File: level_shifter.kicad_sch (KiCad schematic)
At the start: 4 parts, among them U1 TXS0102QDCURQ1

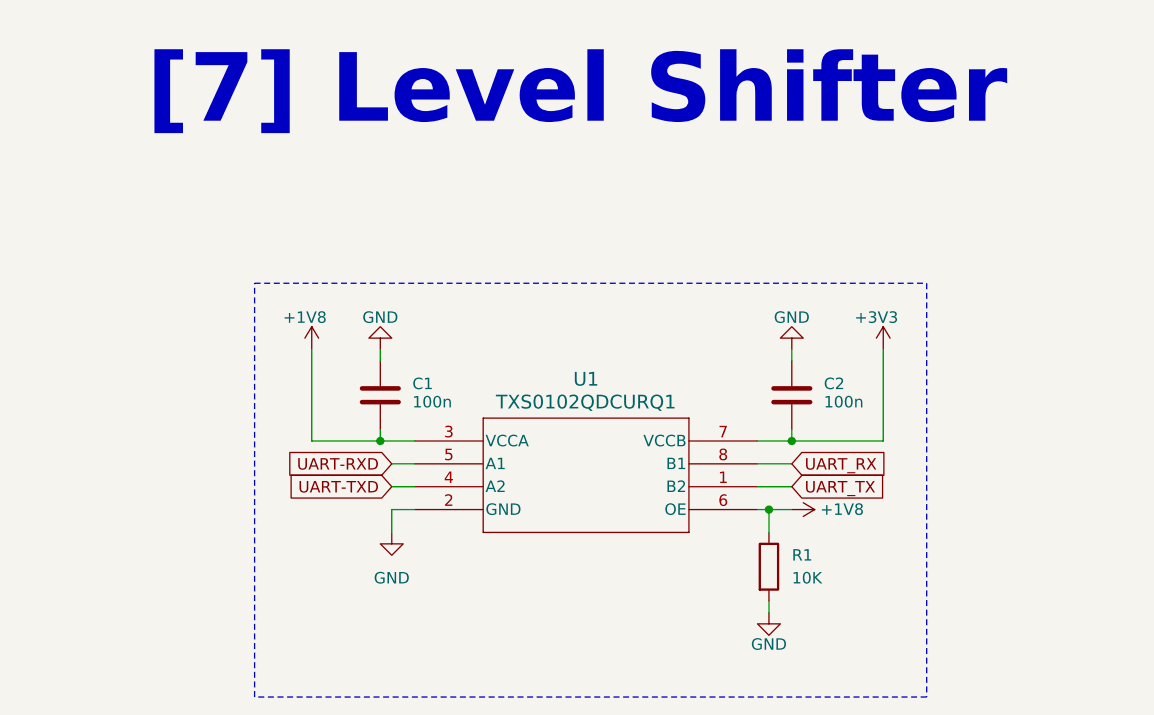
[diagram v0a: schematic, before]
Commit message: Added some decoup caps and reviewed PCB layout
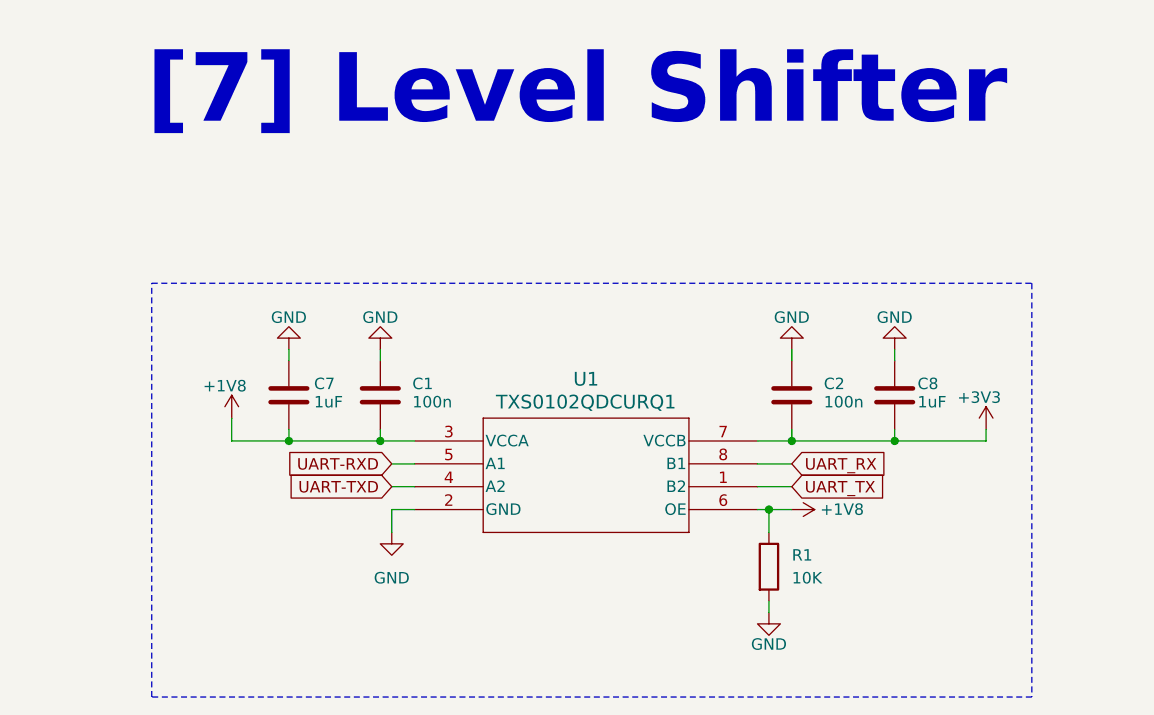
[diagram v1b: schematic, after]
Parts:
- added C7, C8: 1uF, Capacitor_SMD:C_0603_1608Metric, symbol Device:C
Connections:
- net +1V8: now also C7.2
- net +3V3: now also C8.2
- net GND: now also C7.1, C8.1

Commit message: removed some decoup caps because I added to many haha
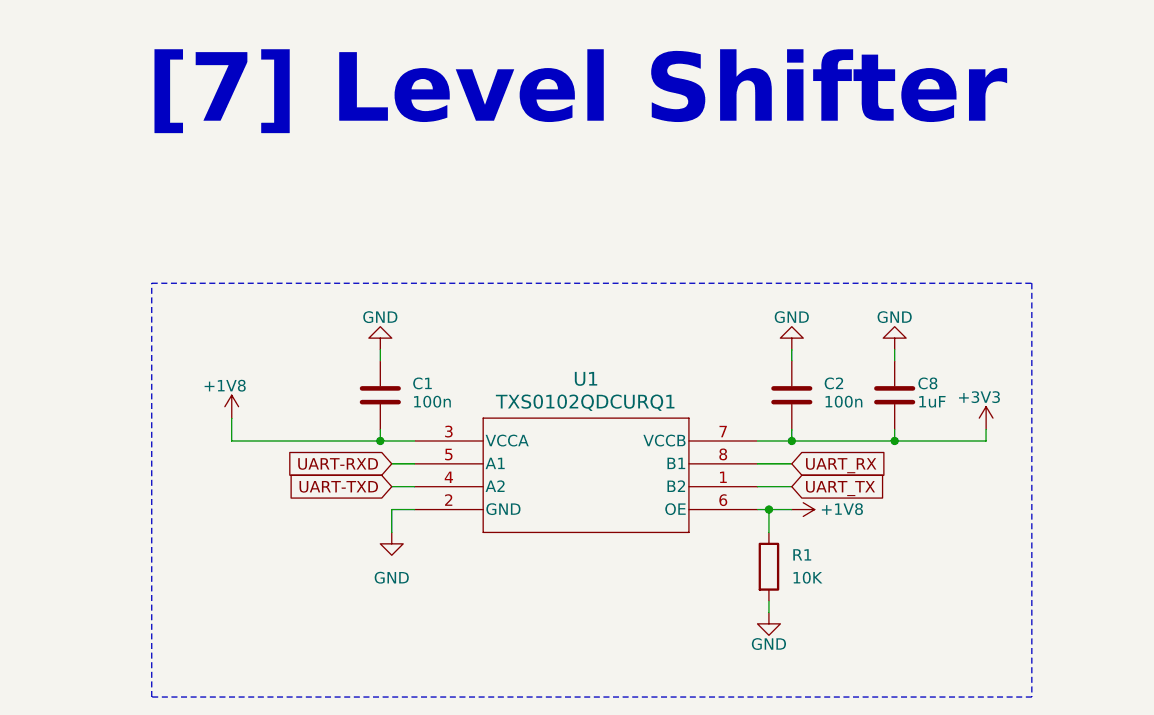
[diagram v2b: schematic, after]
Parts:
- removed C7: 1uF, Capacitor_SMD:C_0603_1608Metric, symbol Device:C
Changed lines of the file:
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@@
 		(color 0 0 0 0)
 	)
-	(junction
-		(at 114.3 69.85)
-		(diameter 0)
-		(color 0 0 0 0)
-	)
 	(wire
 		(pts
@@
 	(wire
 		(pts
-			(xy 114.3 69.85) (xy 124.46 69.85)
+			(xy 107.95 69.85) (xy 124.46 69.85)
 		)
 		(stroke
@@
 	(wire
 		(pts
-			(xy 107.95 69.85) (xy 114.3 69.85)
-		)
-		(stroke
-			(width 0)
-			(type default)
-		)
-	)
-	(wire
-		(pts
 			(xy 166.37 72.39) (xy 170.18 72.39)
 		)
@@
 		(pts
 			(xy 181.61 68.58) (xy 181.61 69.85)
-		)
-		(stroke
-			(width 0)
-			(type default)
-		)
-	)
-	(wire
-		(pts
-			(xy 114.3 59.69) (xy 114.3 60.96)
-		)
-		(stroke
-			(width 0)
-			(type default)
-		)
-	)
-	(wire
-		(pts
-			(xy 114.3 68.58) (xy 114.3 69.85)
 		)
 		(stroke
@@
 	(symbol
 		(lib_id "power:GND")
-		(at 114.3 59.69 180)
-		(unit 1)
-		(body_style 1)
-		(exclude_from_sim no)
-		(in_bom yes)
-		(on_board yes)
-		(in_pos_files yes)
-		(dnp no)
-		(property "Reference" "#PWR046"
-			(at 114.3 53.34 0)
-			(hide yes)
-			(show_name no)
-			(do_not_autoplace no)
-			(effects
-				(font
-					(size 1.27 1.27)
-				)
-			)
-		)
-		(property "Value" "GND"
-			(at 114.3 56.134 0)
-			(show_name no)
-			(do_not_autoplace no)
-			(effects
-				(font
-					(size 1.27 1.27)
-				)
-			)
-		)
-		(property "Footprint" ""
-			(at 114.3 59.69 0)
-			(hide yes)
-			(show_name no)
-			(do_not_autoplace no)
-			(effects
-				(font
-					(size 1.27 1.27)
-				)
-			)
-		)
-		(property "Datasheet" ""
-			(at 114.3 59.69 0)
-			(hide yes)
-			(show_name no)
-			(do_not_autoplace no)
-			(effects
-				(font
-					(size 1.27 1.27)
-				)
-			)
-		)
-		(property "Description" "Power symbol creates a global label with name \"GND\" , ground"
-			(at 114.3 59.69 0)
-			(hide yes)
-			(show_name no)
-			(do_not_autoplace no)
-			(effects
-				(font
-					(size 1.27 1.27)
-				)
-			)
-		)
-		(pin "1"
-		)
-		(instances
-			(project "adapter-pcb"
-				(path "/94da9b83-1146-4f01-8e34-8153765b0257/cf109836-ab8e-48e3-a0ed-36c6666f071e"
-					(reference "#PWR046")
-					(unit 1)
-				)
-			)
-		)
-	)
-	(symbol
-		(lib_id "power:GND")
 		(at 124.46 59.69 180)
 		(unit 1)
@@
 					(unit 1)
 				)
-			)
-		)
-	)
-	(symbol
-		(lib_id "Device:C")
-		(at 114.3 64.77 0)
-		(unit 1)
-		(body_style 1)
-		(exclude_from_sim no)
-		(in_bom yes)
-		(on_board yes)
-		(in_pos_files yes)
-		(dnp no)
-		(property "Reference" "C7"
-			(at 117.094 63.5 0)
-			(show_name no)
-			(do_not_autoplace no)
-			(effects
-				(font
-					(size 1.27 1.27)
-				)
-				(justify left)
-			)
-		)
-		(property "Value" "1uF"
-			(at 117.094 65.532 0)
-			(show_name no)
-			(do_not_autoplace no)
-			(effects
-				(font
-					(size 1.27 1.27)
-				)
-				(justify left)
-			)
-		)
-		(property "Footprint" "Capacitor_SMD:C_0603_1608Metric"
-			(at 115.2652 68.58 0)
-			(hide yes)
-			(show_name no)
-			(do_not_autoplace no)
-			(effects
-				(font
-					(size 1.27 1.27)
-				)
-			)
-		)
-		(property "Datasheet" ""
-			(at 114.3 64.77 0)
-			(hide yes)
-			(show_name no)
-			(do_not_autoplace no)
-			(effects
-				(font
-					(size 1.27 1.27)
-				)
-			)
-		)
-		(property "Description" ""
-			(at 114.3 64.77 0)
-			(hide yes)
-			(show_name no)
-			(do_not_autoplace no)
-			(effects
-				(font
-					(size 1.27 1.27)
-				)
-			)
-		)
-		(property "MANUFACTURER" "Murata Electronics"
-			(at 114.3 64.77 0)
-			(hide yes)
-			(show_name no)
-			(do_not_autoplace no)
-			(effects
-				(font
-					(size 1.27 1.27)
-				)
-			)
-		)
-		(property "MANUFACTURER_PART_NUMBER" "GCM155R71H104KE02D"
-			(at 114.3 64.77 0)
-			(hide yes)
-			(show_name no)
-			(do_not_autoplace no)
-			(effects
-				(font
-					(size 1.27 1.27)
-				)
-			)
-		)
-		(pin "1"
-		)
-		(pin "2"
-		)
-		(instances
-			(project "adapter-pcb"
-				(path "/94da9b83-1146-4f01-8e34-8153765b0257/cf109836-ab8e-48e3-a0ed-36c6666f071e"
-					(reference "C7")
-					(unit 1)
-				)
